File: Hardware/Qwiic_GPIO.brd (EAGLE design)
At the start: 30.5 x 25.4 mm, 26 parts, among them J2 SMD, J3 PTH, J4 SMD, U3 TCA9534U

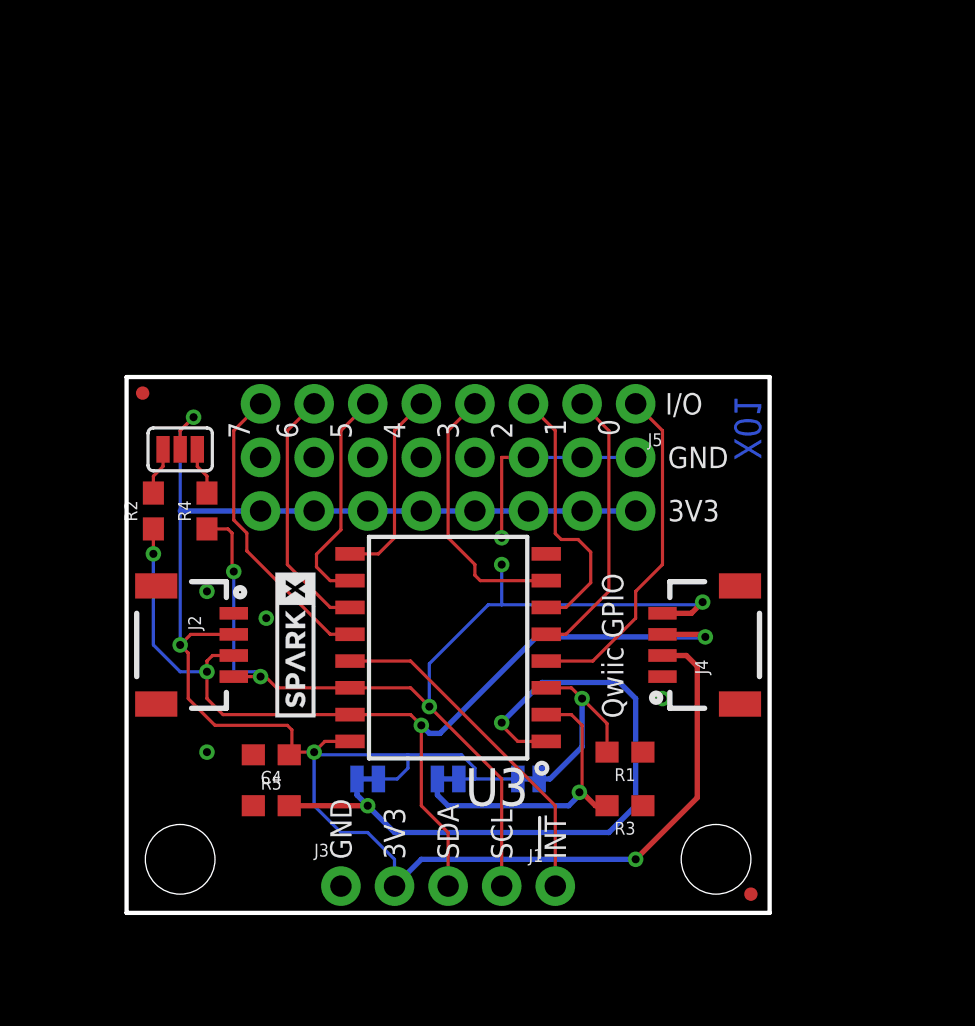
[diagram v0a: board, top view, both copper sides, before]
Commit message: Updated PCB with latch terminals and buzzard labels
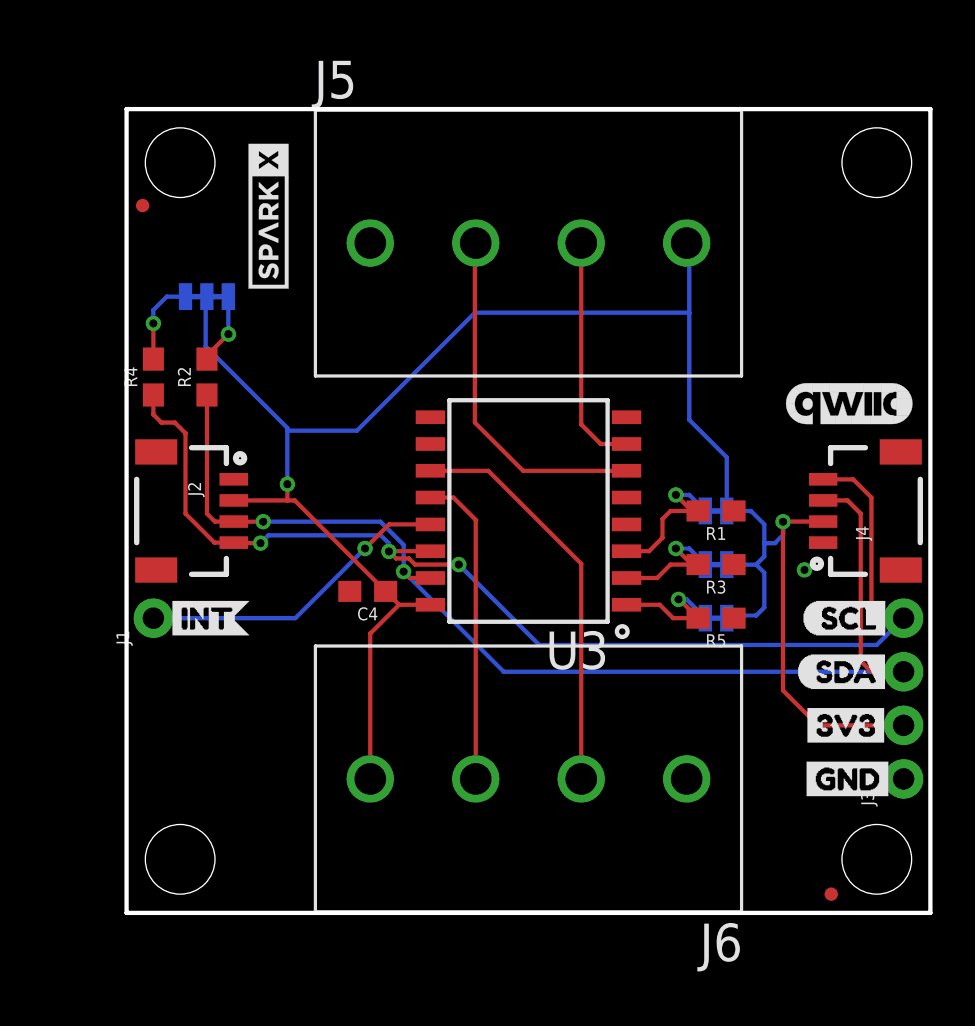
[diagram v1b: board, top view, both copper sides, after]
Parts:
- removed J7: (no value), SparkFun-Connectors:1X08_NO_SILK
- removed SJ5: SMT-JUMPER-_3-2-NC-PASTE_TALL, KevinKuwata_eagle:SMT-JUMPER_3-2-NC-PASTE_SILK_TALLER_A
- added JP10: JUMPER-SMT_3_2-NC_TRACE_SILK, SparkFun-Jumpers:SMT-JUMPER_3_2-NC_TRACE_SILK
- added JP8, JP9: STAND-OFF, SparkFun:STAND-OFF
- added U$10: (no value), buzzard_labels (44):SDA5
- added U$11: (no value), buzzard_labels (45):A00
- added U$12: (no value), buzzard_labels (45):A21
- added U$13: (no value), buzzard_labels (45):INT2
- added U$14, U$15: (no value), buzzard_labels (47):__3V3__3
- added U$16: (no value), buzzard_labels (49):_____1_____1
- added U$17: (no value), buzzard_labels (49):______0______0
- added U$18: (no value), buzzard_labels (48):_____3_____2
- added U$19: (no value), buzzard_labels (48):______2______1
- added U$20: (no value), Labels:I_SUPER2_C-()-03
- added U$21: (no value), SparkFun-Aesthetics:QWIIC_6MM
- added U$22: (no value), buzzard_labels (51):INT2
- added U$23: (no value), buzzard_labels (51):SCL0
- added U$24: (no value), buzzard_labels (51):SDA1
- added U$25, U$7: (no value), buzzard_labels (44):GND4
- added U$26, U$3: (no value), buzzard_labels (44):3V33
- added U$4, U$6: (no value), buzzard_labels (48):__GND__0
- added U$5: (no value), buzzard_labels (44):A11
- added U$8: (no value), buzzard_labels (44):QWIIC_GPIO7
- added U$9: (no value), buzzard_labels (44):SCL6
- J5, J6: device SparkFun-Connectors:1X08_NO_SILK -> SparkFun-Connectors:LATCHTERMINAL-5MM-4
- JP1, JP5, JP7: value JUMPER-SMT_2_NC_TRACE_NO-SILK -> JUMPER-SMT_2_NC_TRACE_SILK; device SparkFun-Jumpers:SMT-JUMPER_2_NC_TRACE_NO-SILK -> SparkFun-Jumpers:SMT-JUMPER_2_NC_TRACE_SILK
- moved J3 27.1 mm to (36.8, 6.35), turned to 90 degrees
- moved J1 22.9 mm to (1.27, 14.0), turned to 90 degrees
- moved R5 22.9 mm to (27.9, 14.0), turned to 180 degrees
- moved U$2 20.4 mm to (6.73, 33.0)
- moved JP7 18.2 mm to (27.9, 14.0)
- moved JP5 16.3 mm to (27.9, 16.5)
- moved J6 16.1 mm to (19.1, 6.35), flipped to the top, turned to 180 degrees
- moved JP1 15.5 mm to (27.9, 19.1), turned to 180 degrees
- moved LOGO1 13.3 mm to (15.2, 17.8)
- moved R3 12.2 mm to (27.9, 16.5)
- moved R1 12.2 mm to (27.9, 19.1)
- moved J4 9.92 mm to (33.0, 19.1)
- moved J5 9.16 mm to (19.1, 31.8), turned to 0 degrees
- moved C4 9.00 mm to (11.4, 15.2)
- moved JP6 8.89 mm to (0.76, 33.5)
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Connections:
- net 3.3V: now also J5.P$4, J6.P$4, JP10.2; no longer J7.1, J7.2, J7.3, J7.4, J7.5, J7.6, J7.7, J7.8, SJ5.2
- net GND: now also J5.P$1, J6.P$1; no longer J6.1, J6.2, J6.3, J6.4, J6.5, J6.6, J6.7, J6.8
- net P0: no longer J5.1
- net P1: no longer J5.2
- net P2: now also J5.P$2; no longer J5.3
- net P3: now also J5.P$3; no longer J5.4
- net P4: no longer J5.5
- net P5: no longer J5.6
- net P6: now also J6.P$2; no longer J5.7
- net P7: now also J6.P$3; no longer J5.8
- net SCL_PU1: now also JP10.1; no longer SJ5.1
- net SDA_PU1: now also JP10.3; no longer SJ5.3
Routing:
- net A0: track 34.0 -> 6.59 mm, vias 2 -> 1
- net P0: track 16.3 -> 0.00 mm
- net P1: track 13.2 -> 0.00 mm
- net P5: track 10.6 -> 0.00 mm
- net GND: track 10.2 -> 0.00 mm, vias 5 -> 1
- net P4: track 9.30 -> 0.00 mm
- net A1: track 14.8 -> 6.74 mm
- net P6: track 12.0 -> 19.2 mm
- net SDA: track 48.1 -> 55.2 mm, vias 4 -> 2
- net SCL: track 49.3 -> 55.9 mm, vias 5 -> 3
- net P2: track 12.8 -> 16.7 mm
- net 3.3V: track 96.4 -> 94.0 mm, vias 4 -> 2
- net A2: track 9.89 -> 7.78 mm
- net SDA_PU1: track 2.26 -> 4.11 mm, vias 0 -> 1
- net P3: track 12.7 -> 11.1 mm
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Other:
- board size 30.5 x 25.4 mm -> 38.1 x 38.1 mm
- board text removed: "!INT"
- board text removed: "0"
- board text removed: "1"
- board text removed: "2"
- board text removed: "3"
- board text removed: "3V3"
- board text removed: "4"
- board text removed: "5"
- board text removed: "6"
- board text removed: "7"
- board text removed: "A0"
- board text removed: "A1"
- board text removed: "A2"
- board text removed: "GND"
- board text removed: "I/O"
- board text removed: "Qwiic GPIO"
- board text removed: "SCL"
- board text removed: "SDA"
- board text removed: "X01"

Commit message: Fixed routing and silk issues. Ready to order rev X02
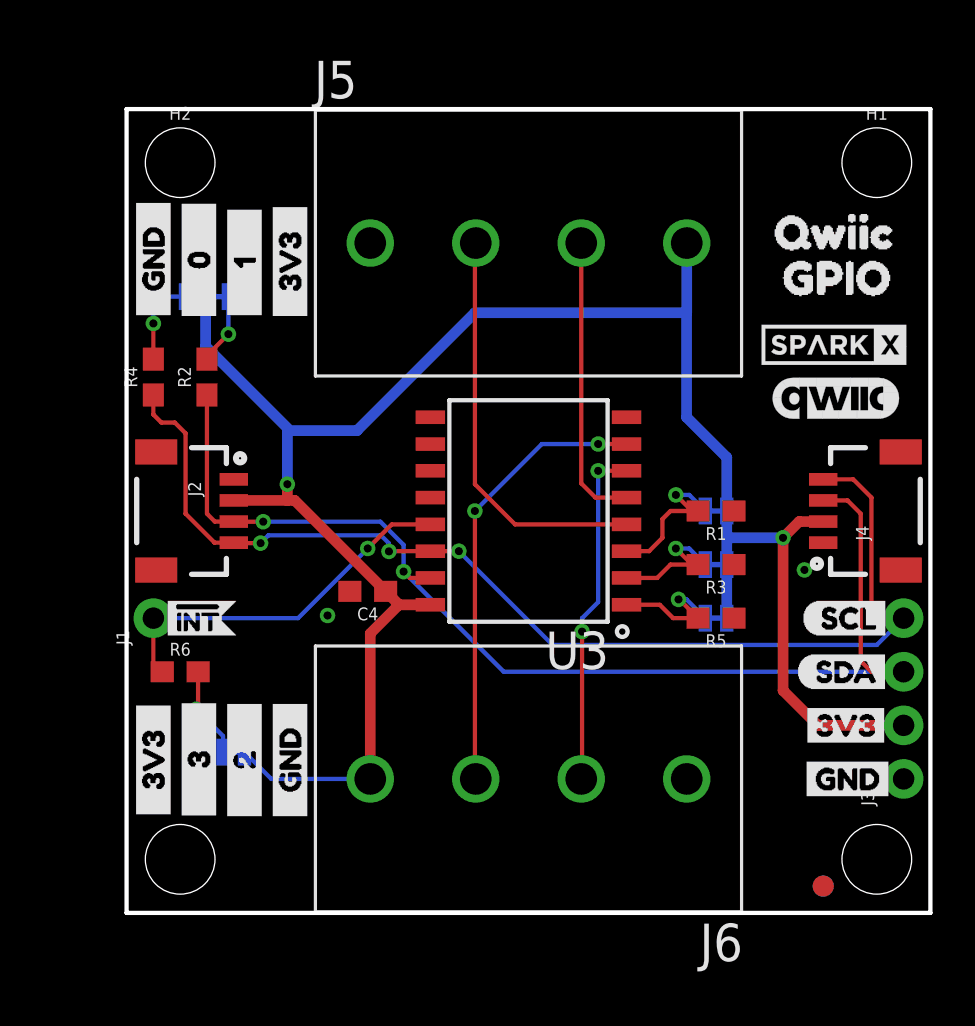
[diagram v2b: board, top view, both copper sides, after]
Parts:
- removed JP9: STAND-OFF, SparkFun:STAND-OFF
- added FD1, FD2: FIDUCIAL1X2, SparkFun-Aesthetics:FIDUCIAL-1X2
- added H1, H2: STAND-OFF, SparkFun-Hardware:STAND-OFF
- added R6: 10k, SparkFun-Resistors:0603
- added U$27, U$29: (no value), buzzard_labels (48):__GND__0
- added U$28: (no value), buzzard_labels (48):_____3_____2
- added U$30, U$34: (no value), buzzard_labels (47):__3V3__3
- added U$31: (no value), buzzard_labels (57):_____2_____0
- added U$32: (no value), buzzard_labels (60):QWIIC1
- added U$33: (no value), buzzard_labels (49):_____1_____1
- added U$35: (no value), buzzard_labels (58):_____0_____0
- added U$36: (no value), buzzard_labels (61):GPIO1
- JP2, JP6: value FIDUCIALUFIDUCIAL -> FIDUCIAL1X2; device SparkFun:MICRO-FIDUCIAL -> SparkFun:FIDUCIAL-1X2
- JP8: value STAND-OFF -> JUMPER-SMT_2_NC_TRACE_SILK; device SparkFun:STAND-OFF -> SparkFun-Jumpers:SMT-JUMPER_2_NC_TRACE_SILK
- R1, R3, R5: value 10k -> 2.2k
- U$13: device buzzard_labels (45):INT2 -> buzzard_labels (52):#INT0
- U$22: device buzzard_labels (51):INT2 -> buzzard_labels (54):#INT0
- moved JP8 28.1 mm to (5.08, 7.62), flipped to the bottom, turned to 180 degrees
- moved U$2 27.5 mm to (33.5, 26.9), turned to 0 degrees
- moved JP6 0.72 mm to (1.27, 33.0)
- moved U$21 0.68 mm to (33.7, 24.4)
- moved JP2 0.54 mm to (33.0, 1.27)
- moved U$13 0.38 mm to (1.27, 14.0)
- moved U$22 0.38 mm to (5.46, 14.0)
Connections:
- new net N$1: JP8.1, R6.2
- net !INT: now also R6.1
- net 3.3V: now also J5.4, J6.4, JP8.2; no longer J5.P$4, J6.P$4
- net GND: now also J5.1, J6.1; no longer J5.P$1, J6.P$1
- net P0: now also J5.2
- net P1: now also J5.3
- net P2: now also J6.2; no longer J5.P$2
- net P3: now also J6.3; no longer J5.P$3
- net P6: no longer J6.P$2
- net P7: no longer J6.P$3
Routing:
- net P0: track 0.00 -> 19.4 mm
- net P6: track 19.2 -> 0.00 mm
- net P7: track 14.9 -> 0.00 mm
- net P1: track 0.00 -> 13.8 mm
- net P3: track 11.1 -> 21.2 mm, vias 0 -> 2
- net N$1: track 0.00 -> 4.37 mm, vias 0 -> 1
- net !INT: track 15.0 -> 17.7 mm
- net 3.3V: track 94.0 -> 96.3 mm
- net SCL: track 55.9 -> 54.0 mm
- net P2: track 16.7 -> 16.3 mm, vias 0 -> 2

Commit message: Change silk to table
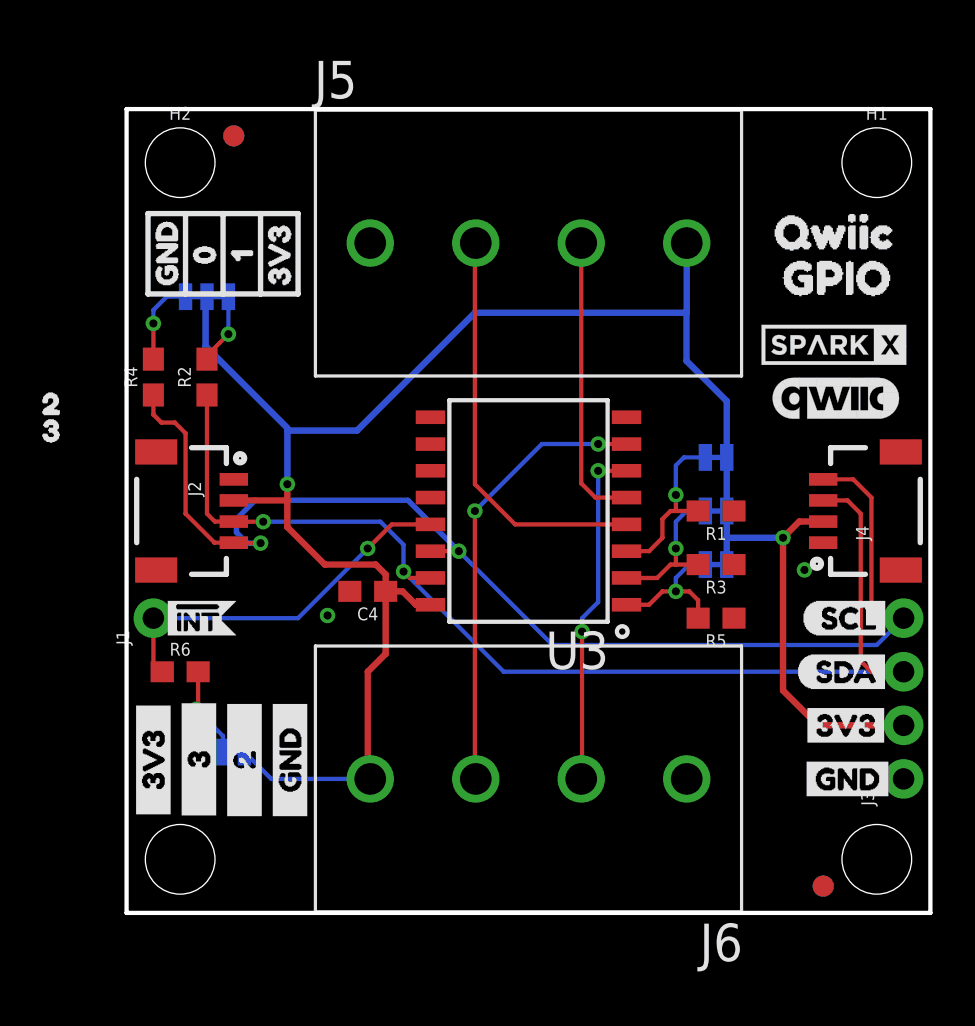
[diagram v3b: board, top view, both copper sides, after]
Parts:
- added U$37: (no value), buzzard_labels (5):04
- added U$38: (no value), buzzard_labels (5):3V33
- JP1, JP5, JP7: value JUMPER-SMT_2_NC_TRACE_SILK -> (none)
- U$29: device buzzard_labels (48):__GND__0 -> buzzard_labels (5):15
- U$33: device buzzard_labels (49):_____1_____1 -> buzzard_labels (5):20
- U$34: device buzzard_labels (47):__3V3__3 -> buzzard_labels (5):31
- U$35: device buzzard_labels (58):_____0_____0 -> buzzard_labels (5):GND2
- moved LOGO1 17.6 mm to (6.35, 2.54)
- moved U$34 13.8 mm to (-5.08, 22.9), turned to 0 degrees
- moved U$33 11.3 mm to (-5.08, 24.1), turned to 0 degrees
- moved JP7 7.62 mm to (27.9, 21.6)
- moved FD1 5.39 mm to (5.08, 36.8)
- moved JP6 5.39 mm to (5.08, 36.8)
- moved U$29 4.71 mm to (5.46, 30.0)
- moved U$11 2.54 mm to (33.0, 16.5)
- moved JP1 2.54 mm to (27.9, 16.5)
- moved JP5 2.54 mm to (27.9, 19.1)
- moved U$12 2.54 mm to (33.0, 21.6)
- moved U$5 2.54 mm to (33.0, 19.1)
- moved U$35 1.83 mm to (1.91, 28.8)
- moved U$1 1.27 mm to (19.1, 17.8)
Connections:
- removed net P4: U3.9
- removed net P5: U3.10
- removed net P6: U3.11
- removed net P7: U3.12
- net A0: now also JP1.1; no longer JP7.1
- net A2: now also JP7.1; no longer JP1.1
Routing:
- net SCL: track 54.0 -> 59.1 mm, vias 3 -> 2
- net A2: track 7.78 -> 8.71 mm
- net 3.3V: track 96.3 -> 95.4 mm
- net A1: track 6.74 -> 7.29 mm
- net A0: track 6.59 -> 7.10 mm

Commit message: Silkscreen
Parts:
- removed U$30: (no value), buzzard_labels (47):__3V3__3
- removed U$31: (no value), buzzard_labels (57):_____2_____0
- U$27: device buzzard_labels (48):__GND__0 -> buzzard_labels (62):3V32
- U$28: device buzzard_labels (48):_____3_____2 -> buzzard_labels (62):GND1
- moved U$33 20.6 mm to (3.56, 5.46), turned to 90 degrees
- moved U$34 20.2 mm to (5.21, 5.46), turned to 90 degrees
- moved U$27 6.00 mm to (1.78, 4.70)
- moved U$28 3.74 mm to (7.11, 4.57)
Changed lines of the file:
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@@
 <?xml version="1.0" encoding="utf-8"?>
 <!DOCTYPE eagle SYSTEM "eagle.dtd">
-<eagle version="9.5.2">
+<eagle version="9.4.2">
 <drawing>
 <settings>
@@
 <layer number="47" name="Measures" color="7" fill="1" visible="no" active="yes"/>
 <layer number="48" name="Document" color="7" fill="1" visible="no" active="yes"/>
-<layer number="49" name="Reference" color="7" fill="1" visible="yes" active="yes"/>
+<layer number="49" name="Reference" color="7" fill="1" visible="no" active="yes"/>
 <layer number="50" name="dxf" color="7" fill="1" visible="no" active="yes"/>
 <layer number="51" name="tDocu" color="6" fill="1" visible="yes" active="yes"/>
@@
 <wire x1="1.016" y1="29.337" x2="1.016" y2="33.147" width="0.254" layer="21"/>
 <wire x1="1.016" y1="33.147" x2="2.794" y2="33.147" width="0.254" layer="21"/>
+<wire x1="0.762" y1="5.08" x2="2.667" y2="5.08" width="0.254" layer="21"/>
+<wire x1="2.667" y1="5.08" x2="4.445" y2="5.08" width="0.254" layer="21"/>
+<wire x1="4.445" y1="5.08" x2="6.096" y2="5.08" width="0.254" layer="21"/>
+<wire x1="6.096" y1="5.08" x2="8.128" y2="5.08" width="0.254" layer="21"/>
+<wire x1="8.128" y1="5.08" x2="8.128" y2="8.89" width="0.254" layer="21"/>
+<wire x1="8.128" y1="8.89" x2="4.445" y2="8.89" width="0.254" layer="21"/>
+<wire x1="4.445" y1="8.89" x2="2.667" y2="8.89" width="0.254" layer="21"/>
+<wire x1="2.667" y1="8.89" x2="0.762" y2="8.89" width="0.254" layer="21"/>
+<wire x1="0.762" y1="8.89" x2="0.762" y2="5.08" width="0.254" layer="21"/>
+<wire x1="6.096" y1="8.763" x2="6.096" y2="5.08" width="0.254" layer="21"/>
+<wire x1="2.667" y1="8.89" x2="2.667" y2="5.08" width="0.254" layer="21"/>
+<wire x1="4.445" y1="8.89" x2="4.445" y2="5.08" width="0.254" layer="21"/>
 </plain>
 <attributes>
@@
 <attribute name="VALUE" x="5.08" y="8.763" size="0.6096" layer="28" font="vector" ratio="20" rot="MR180" align="top-center"/>
 </element>
-<element name="U$27" library="buzzard_labels (48)" package="__GND__0" value="" x="7.747" y="4.064" smashed="yes" rot="R90"/>
-<element name="U$28" library="buzzard_labels (48)" package="_____3_____2" value="" x="3.429" y="3.937" smashed="yes" rot="R90"/>
-<element name="U$30" library="buzzard_labels (47)" package="__3V3__3" value="" x="1.27" y="4.191" smashed="yes" rot="R90"/>
-<element name="U$31" library="buzzard_labels (57)" package="_____2_____0" value="" x="5.588" y="4.064" smashed="yes" rot="R90"/>
 <element name="U$32" library="buzzard_labels (60)" package="QWIIC1" value="" x="29.337" y="32.258" smashed="yes"/>
 <element name="U$36" library="buzzard_labels (61)" package="GPIO1" value="" x="29.718" y="30.099" smashed="yes"/>
 <element name="U$37" library="buzzard_labels (5)" package="04" value="" x="3.683" y="29.845" smashed="yes" rot="R90"/>
 <element name="U$29" library="buzzard_labels (5)" package="15" value="" x="5.461" y="29.972" smashed="yes" rot="R90"/>
-<element name="U$33" library="buzzard_labels (5)" package="20" value="" x="-5.08" y="24.13" smashed="yes"/>
-<element name="U$34" library="buzzard_labels (5)" package="31" value="" x="-5.08" y="22.86" smashed="yes"/>
+<element name="U$33" library="buzzard_labels (5)" package="20" value="" x="3.556" y="5.461" smashed="yes" rot="R90"/>
+<element name="U$34" library="buzzard_labels (5)" package="31" value="" x="5.207" y="5.461" smashed="yes" rot="R90"/>
 <element name="U$35" library="buzzard_labels (5)" package="GND2" value="" x="1.905" y="28.829" smashed="yes" rot="R90"/>
 <element name="U$38" library="buzzard_labels (5)" package="3V33" value="" x="7.239" y="28.829" smashed="yes" rot="R90"/>
@@
 <attribute name="VALUE" x="27.94" y="22.733" size="0.6096" layer="28" font="vector" ratio="20" rot="MR180" align="top-center"/>
 </element>
+<element name="U$27" library="buzzard_labels (62)" package="3V32" value="" x="1.778" y="4.699" smashed="yes" rot="R90"/>
+<element name="U$28" library="buzzard_labels (62)" package="GND1" value="" x="7.112" y="4.572" smashed="yes" rot="R90"/>
 </elements>
 <signals>
@@
 </signal>
 <signal name="GND">
-<contactref element="J2" pad="1"/>
-<contactref element="J3" pad="1"/>
-<contactref element="C4" pad="2"/>
-<contactref element="J4" pad="1"/>
-<contactref element="R1" pad="1"/>
-<contactref element="R3" pad="1"/>
-<contactref element="R5" pad="1"/>
 <polygon width="0.2032" layer="1" isolate="0.3048">
 <vertex x="0" y="38.1"/>
@@
 <via x="9.525" y="14.097" extent="1-16" drill="0.381"/>
 <contactref element="U3" pad="8"/>
+<contactref element="R1" pad="1"/>
+<contactref element="R3" pad="1"/>
+<contactref element="R5" pad="1"/>
+<contactref element="J4" pad="1"/>
+<contactref element="J3" pad="1"/>
+<contactref element="J2" pad="1"/>
+<contactref element="C4" pad="2"/>
 </signal>
 <signal name="SCL_PU1">
